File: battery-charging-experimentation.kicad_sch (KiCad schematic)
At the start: 23 parts, among them J1 USB_C_Receptacle_PowerOnly_6P, Q1 FS8205A, Q2 AO3415A, U2 DW01, U3 TP4056-42-ESOP8

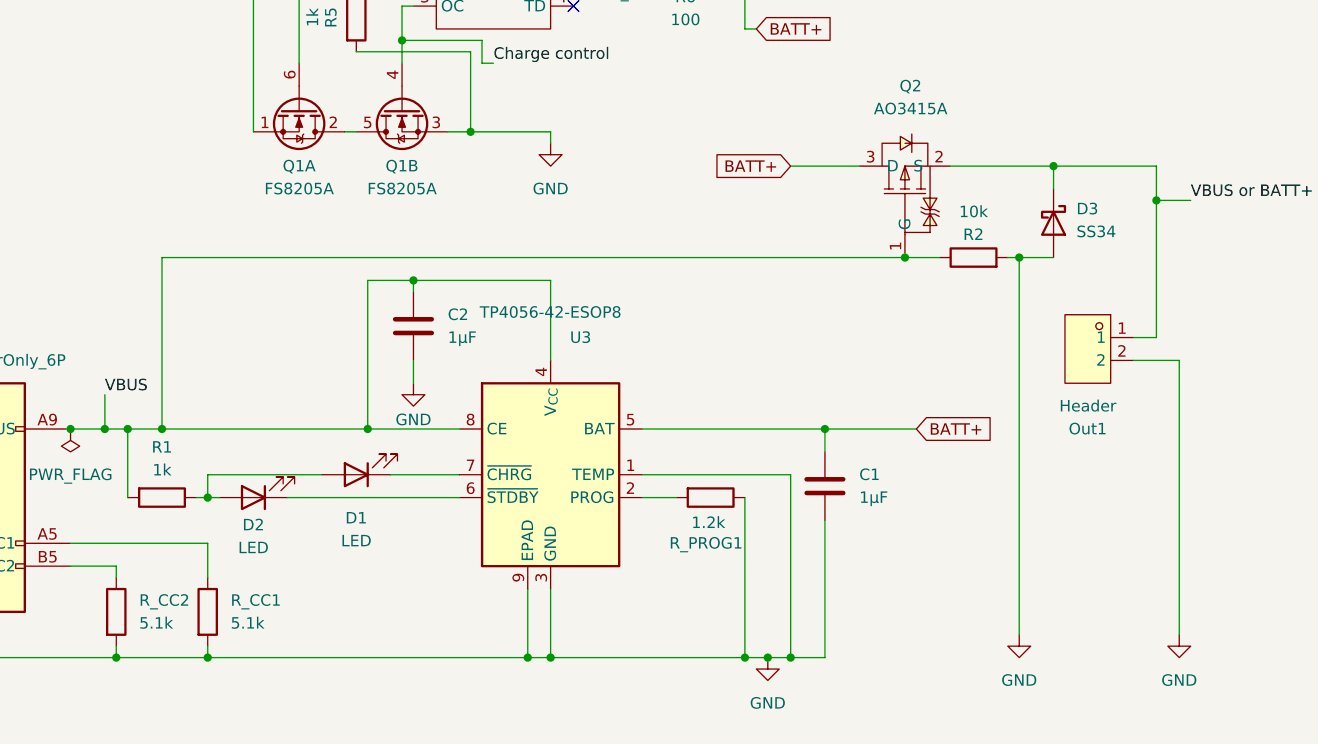
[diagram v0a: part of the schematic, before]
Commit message: move diode so the thing actually works
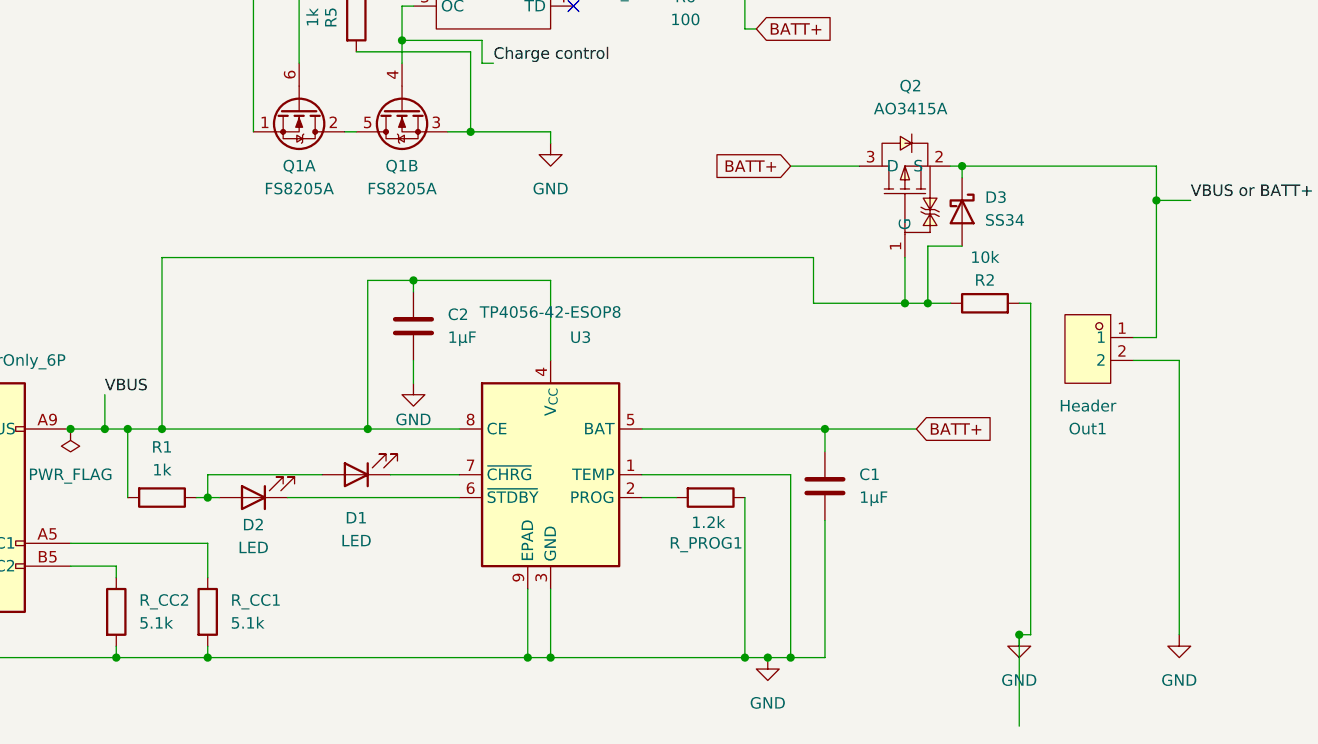
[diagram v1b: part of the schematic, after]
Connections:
- net GND: no longer D3.2 (A)
- net VBUS: now also D3.2 (A)
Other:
- title: (none) -> Chargey board
- moved on the sheet: D3, R2
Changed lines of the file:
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@@
 	(generator_version "9.0")
 	(paper "A4")
+	(title_block
+		(title "Chargey board")
+		(rev "2")
+	)
 	(junction
 		(at 33.02 190.5)
@@
 	)
 	(junction
-		(at 153.67 146.05)
-		(diameter 0)
-		(color 0 0 0 0)
-	)
-	(junction
 		(at 74.93 110.49)
 		(diameter 0)
@@
 	)
 	(junction
-		(at 140.97 146.05)
+		(at 143.51 151.13)
 		(diameter 0)
 		(color 0 0 0 0)
@@
 	)
 	(junction
-		(at 157.48 135.89)
+		(at 147.32 135.89)
 		(diameter 0)
 		(color 0 0 0 0)
@@
 	)
 	(junction
+		(at 153.67 187.96)
+		(diameter 0)
+		(color 0 0 0 0)
+	)
+	(junction
 		(at 101.6 190.5)
 		(diameter 0)
@@
 	)
 	(junction
+		(at 140.97 151.13)
+		(diameter 0)
+		(color 0 0 0 0)
+	)
+	(junction
 		(at 52.07 165.1)
 		(diameter 0)
@@
 	(wire
 		(pts
+			(xy 147.32 135.89) (xy 168.91 135.89)
+		)
+		(stroke
+			(width 0)
+			(type default)
+		)
+	)
+	(wire
+		(pts
 			(xy 68.58 102.87) (xy 68.58 132.08)
 		)
@@
 	(wire
 		(pts
-			(xy 146.05 135.89) (xy 157.48 135.89)
+			(xy 154.94 187.96) (xy 153.67 187.96)
 		)
 		(stroke
@@
 	(wire
 		(pts
-			(xy 90.17 132.08) (xy 92.71 132.08)
+			(xy 146.05 135.89) (xy 147.32 135.89)
 		)
 		(stroke
@@
 	(wire
 		(pts
-			(xy 123.19 120.65) (xy 123.19 114.3)
+			(xy 90.17 132.08) (xy 92.71 132.08)
 		)
 		(stroke
@@
 	(wire
 		(pts
-			(xy 93.98 121.92) (xy 85.09 121.92)
+			(xy 123.19 120.65) (xy 123.19 114.3)
 		)
 		(stroke
@@
 	(wire
 		(pts
-			(xy 157.48 146.05) (xy 153.67 146.05)
+			(xy 93.98 121.92) (xy 85.09 121.92)
 		)
 		(stroke
@@
 	(wire
 		(pts
+			(xy 147.32 144.78) (xy 143.51 144.78)
+		)
+		(stroke
+			(width 0)
+			(type default)
+		)
+	)
+	(wire
+		(pts
 			(xy 73.66 110.49) (xy 73.66 124.46)
 		)
@@
 	(wire
 		(pts
-			(xy 153.67 146.05) (xy 153.67 187.96)
+			(xy 143.51 144.78) (xy 143.51 151.13)
 		)
 		(stroke
@@
 	(wire
 		(pts
-			(xy 58.42 146.05) (xy 58.42 165.1)
+			(xy 130.81 146.05) (xy 130.81 151.13)
 		)
 		(stroke
@@
 	(wire
 		(pts
-			(xy 80.01 114.3) (xy 86.36 114.3)
+			(xy 58.42 146.05) (xy 58.42 165.1)
 		)
 		(stroke
@@
 	(wire
 		(pts
-			(xy 157.48 135.89) (xy 168.91 135.89)
+			(xy 80.01 114.3) (xy 86.36 114.3)
 		)
 		(stroke
@@
 	(wire
 		(pts
-			(xy 157.48 138.43) (xy 157.48 135.89)
+			(xy 147.32 137.16) (xy 147.32 135.89)
 		)
 		(stroke
@@
 	(wire
 		(pts
+			(xy 146.05 151.13) (xy 143.51 151.13)
+		)
+		(stroke
+			(width 0)
+			(type default)
+		)
+	)
+	(wire
+		(pts
+			(xy 130.81 151.13) (xy 140.97 151.13)
+		)
+		(stroke
+			(width 0)
+			(type default)
+		)
+	)
+	(wire
+		(pts
+			(xy 154.94 151.13) (xy 153.67 151.13)
+		)
+		(stroke
+			(width 0)
+			(type default)
+		)
+	)
+	(wire
+		(pts
 			(xy 132.08 190.5) (xy 128.27 190.5)
 		)
@@
 	(wire
 		(pts
-			(xy 140.97 146.05) (xy 144.78 146.05)
+			(xy 99.06 182.88) (xy 99.06 190.5)
 		)
 		(stroke
@@
 	(wire
 		(pts
-			(xy 99.06 182.88) (xy 99.06 190.5)
+			(xy 95.25 124.46) (xy 93.98 124.46)
 		)
 		(stroke
@@
 	(wire
 		(pts
-			(xy 95.25 124.46) (xy 93.98 124.46)
+			(xy 73.66 110.49) (xy 74.93 110.49)
 		)
 		(stroke
@@
 	(wire
 		(pts
-			(xy 73.66 110.49) (xy 74.93 110.49)
+			(xy 140.97 151.13) (xy 140.97 146.05)
 		)
 		(stroke
@@
 	(wire
 		(pts
-			(xy 58.42 146.05) (xy 140.97 146.05)
+			(xy 153.67 198.12) (xy 153.67 187.96)
 		)
 		(stroke
@@
 	(wire
 		(pts
+			(xy 58.42 146.05) (xy 130.81 146.05)
+		)
+		(stroke
+			(width 0)
+			(type default)
+		)
+	)
+	(wire
+		(pts
+			(xy 154.94 151.13) (xy 154.94 187.96)
+		)
+		(stroke
+			(width 0)
+			(type default)
+		)
+	)
+	(wire
+		(pts
 			(xy 52.07 161.29) (xy 52.07 165.1)
 		)
@@
 	(wire
 		(pts
-			(xy 152.4 146.05) (xy 153.67 146.05)
+			(xy 80.01 123.19) (xy 92.71 123.19)
 		)
 		(stroke
@@
 	(wire
 		(pts
-			(xy 80.01 123.19) (xy 92.71 123.19)
+			(xy 125.73 190.5) (xy 128.27 190.5)
 		)
 		(stroke
@@
 	(wire
 		(pts
-			(xy 125.73 190.5) (xy 128.27 190.5)
+			(xy 109.22 102.87) (xy 111.76 102.87)
 		)
 		(stroke
@@
 	(wire
 		(pts
-			(xy 109.22 102.87) (xy 111.76 102.87)
+			(xy 53.34 189.23) (xy 53.34 190.5)
 		)
 		(stroke
@@
 	(wire
 		(pts
-			(xy 53.34 189.23) (xy 53.34 190.5)
+			(xy 63.5 177.8) (xy 63.5 181.61)
 		)
 		(stroke
@@
 	(wire
 		(pts
-			(xy 63.5 177.8) (xy 63.5 181.61)
+			(xy 101.6 157.48) (xy 101.6 148.59)
 		)
 		(stroke
@@
 	(wire
 		(pts
-			(xy 101.6 157.48) (xy 101.6 148.59)
+			(xy 63.5 172.72) (xy 64.77 172.72)
 		)
 		(stroke
@@
 	(wire
 		(pts
-			(xy 63.5 172.72) (xy 64.77 172.72)
+			(xy 143.51 151.13) (xy 140.97 151.13)
 		)
 		(stroke
@@
 	(symbol
 		(lib_id "Diode:SS34")
-		(at 157.48 142.24 270)
+		(at 147.32 140.97 270)
 		(unit 1)
 		(exclude_from_sim no)
@@
 		(fields_autoplaced yes)
 		(property "Reference" "D3"
-			(at 160.02 140.6524 90)
+			(at 149.86 139.3824 90)
 			(effects
 				(font
@@
 		)
 		(property "Value" "SS34"
-			(at 160.02 143.1924 90)
+			(at 149.86 141.9224 90)
 			(effects
 				(font
@@
 		)
 		(property "Footprint" "easyeda2kicad:SMA_L4.3-W2.6-LS5.2-RD"
-			(at 153.035 142.24 0)
+			(at 142.875 140.97 0)
 			(effects
 				(font
@@
 		)
 		(property "Datasheet" "https://www.vishay.com/docs/88751/ss32.pdf"
-			(at 157.48 142.24 0)
+			(at 147.32 140.97 0)
 			(effects
 				(font
@@
 		)
 		(property "Description" "40V 3A Schottky Diode, SMA"
-			(at 157.48 142.24 0)
+			(at 147.32 140.97 0)
 			(effects
 				(font
@@
 		)
 		(property "LCSC Part" "C8678"
-			(at 157.48 142.24 90)
+			(at 147.32 140.97 90)
 			(effects
 				(font
@@
 	(symbol
 		(lib_id "Device:R")
-		(at 148.59 146.05 90)
+		(at 149.86 151.13 90)
 		(unit 1)
 		(exclude_from_sim no)
@@
 		(dnp no)
 		(property "Reference" "R2"
-			(at 148.59 143.51 90)
+			(at 149.86 148.59 90)
 			(effects
 				(font
@@
 		)
 		(property "Value" "10k"
-			(at 148.59 140.97 90)
+			(at 149.86 146.05 90)
 			(effects
 				(font
@@
 		)
 		(property "Footprint" "Resistor_SMD:R_0805_2012Metric_Pad1.20x1.40mm_HandSolder"
-			(at 148.59 147.828 90)
+			(at 149.86 152.908 90)
 			(effects
 				(font
@@
 		)
 		(property "Datasheet" "~"
-			(at 148.59 146.05 0)
+			(at 149.86 151.13 0)
 			(effects
 				(font
@@
 		)
 		(property "Description" "Resistor"
-			(at 148.59 146.05 0)
+			(at 149.86 151.13 0)
 			(effects
 				(font
@@
 		)
 		(property "LCSC Part" "C17414"
-			(at 148.59 146.05 90)
+			(at 149.86 151.13 90)
 			(effects
 				(font

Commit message: add a vbus out pin
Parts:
- Out1: footprint easyeda2kicad:HDR-TH_2P-P2.54-V-M -> Connector_PinHeader_2.54mm:PinHeader_1x03_P2.54mm_Vertical; symbol easyeda2kicad:HXPH254-01-02-Z-L11.5MALEHEADERCONNECTOR -> Connector:Conn_01x03_Pin
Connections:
- net VBUS: now also Out1.3 (Pin_3)
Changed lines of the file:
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@@
-	)
-	(junction
-		(at 168.91 139.7)
-		(diameter 0)
-		(color 0 0 0 0)
 	)
 	(junction
@@
 	)
 	(junction
+		(at 163.83 139.7)
+		(diameter 0)
+		(color 0 0 0 0)
+	)
+	(junction
 		(at 143.51 151.13)
 		(diameter 0)
@@
 	)
 	(junction
+		(at 130.81 151.13)
+		(diameter 0)
+		(color 0 0 0 0)
+	)
+	(junction
 		(at 123.19 102.87)
 		(diameter 0)
@@
 	)
 	(junction
-		(at 153.67 187.96)
-		(diameter 0)
-		(color 0 0 0 0)
-	)
-	(junction
 		(at 101.6 190.5)
 		(diameter 0)
@@
 	(wire
 		(pts
+			(xy 171.45 156.21) (xy 173.99 156.21)
+		)
+		(stroke
+			(width 0)
+			(type default)
+		)
+	)
+	(wire
+		(pts
 			(xy 123.19 106.68) (xy 123.19 102.87)
 		)
@@
 	(wire
 		(pts
+			(xy 171.45 156.21) (xy 171.45 187.96)
+		)
+		(stroke
+			(width 0)
+			(type default)
+		)
+	)
+	(wire
+		(pts
 			(xy 101.6 182.88) (xy 101.6 190.5)
 		)
@@
 	(wire
 		(pts
-			(xy 147.32 135.89) (xy 168.91 135.89)
+			(xy 147.32 135.89) (xy 163.83 135.89)
 		)
 		(stroke
@@
 	(wire
 		(pts
+			(xy 130.81 151.13) (xy 130.81 158.75)
+		)
+		(stroke
+			(width 0)
+			(type default)
+		)
+	)
+	(wire
+		(pts
 			(xy 90.17 132.08) (xy 92.71 132.08)
 		)
@@
 	(wire
 		(pts
-			(xy 171.45 187.96) (xy 171.45 157.48)
-		)
-		(stroke
-			(width 0)
-			(type default)
-		)
-	)
-	(wire
-		(pts
 			(xy 72.39 172.72) (xy 91.44 172.72)
 		)
@@
 	(wire
 		(pts
-			(xy 168.91 154.94) (xy 168.91 139.7)
+			(xy 163.83 153.67) (xy 163.83 139.7)
 		)
 		(stroke
@@
 	(wire
 		(pts
-			(xy 153.67 198.12) (xy 153.67 187.96)
-		)
-		(stroke
-			(width 0)
-			(type default)
-		)
-	)
-	(wire
-		(pts
-			(xy 168.91 154.94) (xy 166.37 154.94)
-		)
-		(stroke
-			(width 0)
-			(type default)
-		)
-	)
-	(wire
-		(pts
 			(xy 58.42 146.05) (xy 130.81 146.05)
 		)
@@
 	(wire
 		(pts
-			(xy 168.91 139.7) (xy 172.72 139.7)
-		)
-		(stroke
-			(width 0)
-			(type default)
-		)
-	)
-	(wire
-		(pts
 			(xy 25.4 190.5) (xy 33.02 190.5)
 		)
@@
 	(wire
 		(pts
-			(xy 171.45 157.48) (xy 166.37 157.48)
-		)
-		(stroke
-			(width 0)
-			(type default)
-		)
-	)
-	(wire
-		(pts
 			(xy 132.08 165.1) (xy 142.24 165.1)
 		)
@@
 	(wire
 		(pts
+			(xy 163.83 139.7) (xy 172.72 139.7)
+		)
+		(stroke
+			(width 0)
+			(type default)
+		)
+	)
+	(wire
+		(pts
 			(xy 53.34 190.5) (xy 63.5 190.5)
 		)
@@
 	(wire
 		(pts
+			(xy 130.81 158.75) (xy 173.99 158.75)
+		)
+		(stroke
+			(width 0)
+			(type default)
+		)
+	)
+	(wire
+		(pts
 			(xy 48.26 165.1) (xy 52.07 165.1)
 		)
@@
 	(wire
 		(pts
-			(xy 168.91 139.7) (xy 168.91 135.89)
+			(xy 163.83 139.7) (xy 163.83 135.89)
 		)
 		(stroke
@@
 		(pts
 			(xy 101.6 157.48) (xy 101.6 148.59)
+		)
+		(stroke
+			(width 0)
+			(type default)
+		)
+	)
+	(wire
+		(pts
+			(xy 163.83 153.67) (xy 173.99 153.67)
 		)
 		(stroke
@@
 	)
 	(symbol
-		(lib_id "easyeda2kicad:HXPH254-01-02-Z-L11.5MALEHEADERCONNECTOR")
-		(at 161.29 156.21 0)
+		(lib_id "Connector:Conn_01x03_Pin")
+		(at 179.07 156.21 0)
 		(mirror y)
 		(unit 1)
@@
 		(dnp no)
 		(property "Reference" "Out1"
-			(at 161.29 165.1 0)
+			(at 179.07 165.1 0)
 			(effects
 				(font
@@
 		)
 		(property "Value" "Header"
-			(at 161.29 162.56 0)
+			(at 179.07 162.56 0)
 			(effects
 				(font
@@
 			)
 		)
-		(property "Footprint" "easyeda2kicad:HDR-TH_2P-P2.54-V-M"
-			(at 161.29 165.1 0)
+		(property "Footprint" "Connector_PinHeader_2.54mm:PinHeader_1x03_P2.54mm_Vertical"
+			(at 179.07 156.21 0)
 			(effects
 				(font
@@
 			)
 		)
-		(property "Datasheet" ""
-			(at 161.29 156.21 0)
+		(property "Datasheet" "~"
+			(at 179.07 156.21 0)
 			(effects
 				(font
@@
 			)
 		)
-		(property "Description" ""
-			(at 161.29 156.21 0)
+		(property "Description" "Generic connector, single row, 01x03, script generated"
+			(at 179.07 156.21 0)
 			(effects
 				(font
@@
 		)
 		(property "LCSC Part" "C52016390"
-			(at 161.29 167.64 0)
+			(at 179.07 167.64 0)
 			(effects
 				(font
@@
 		(pin "2"
 		)
+		(pin "3"
+		)
 		(instances

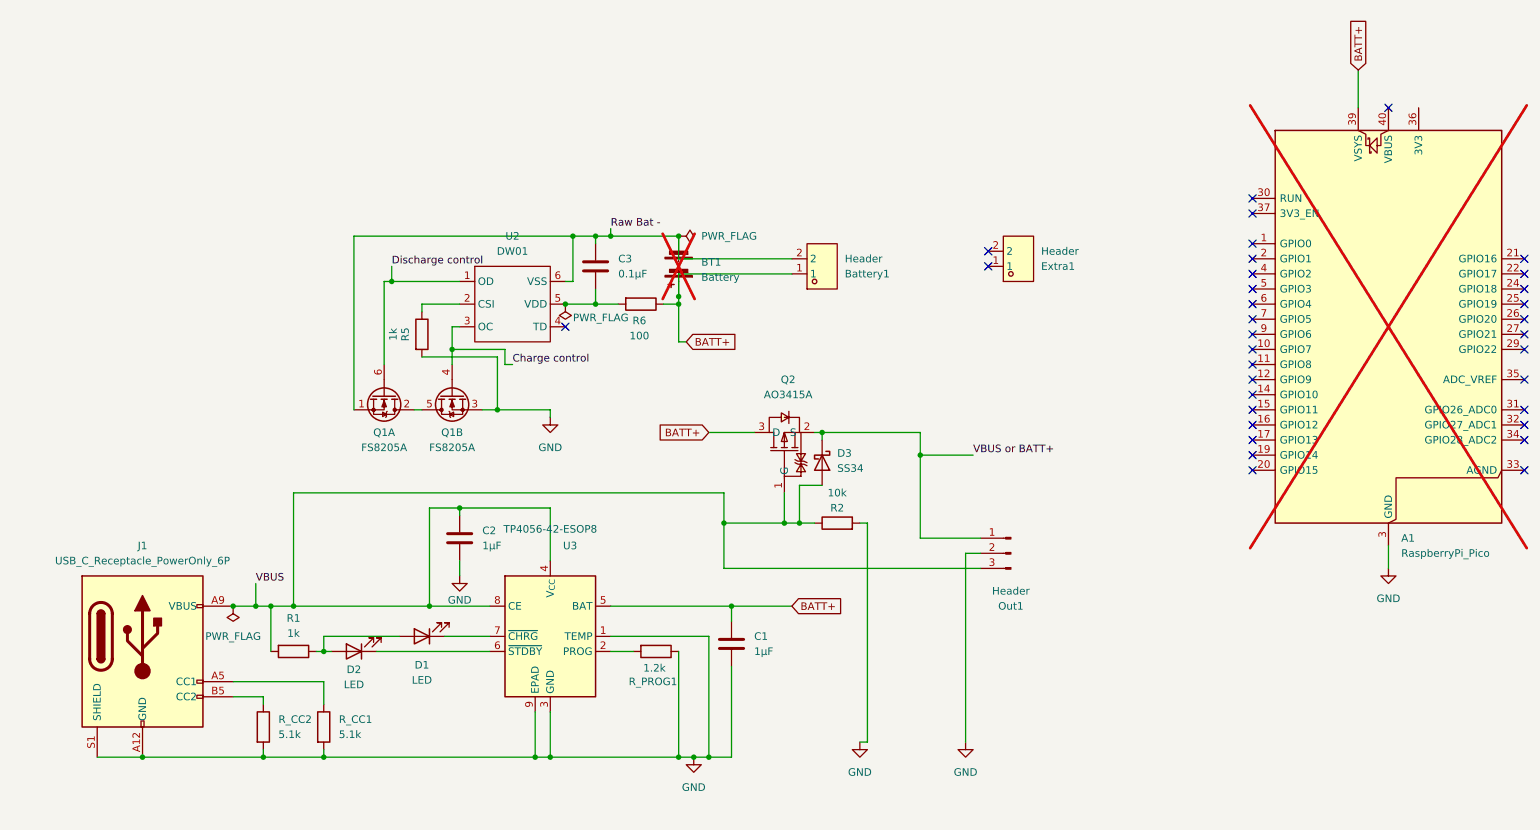
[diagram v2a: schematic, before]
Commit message: smaller components, power from pico USB port
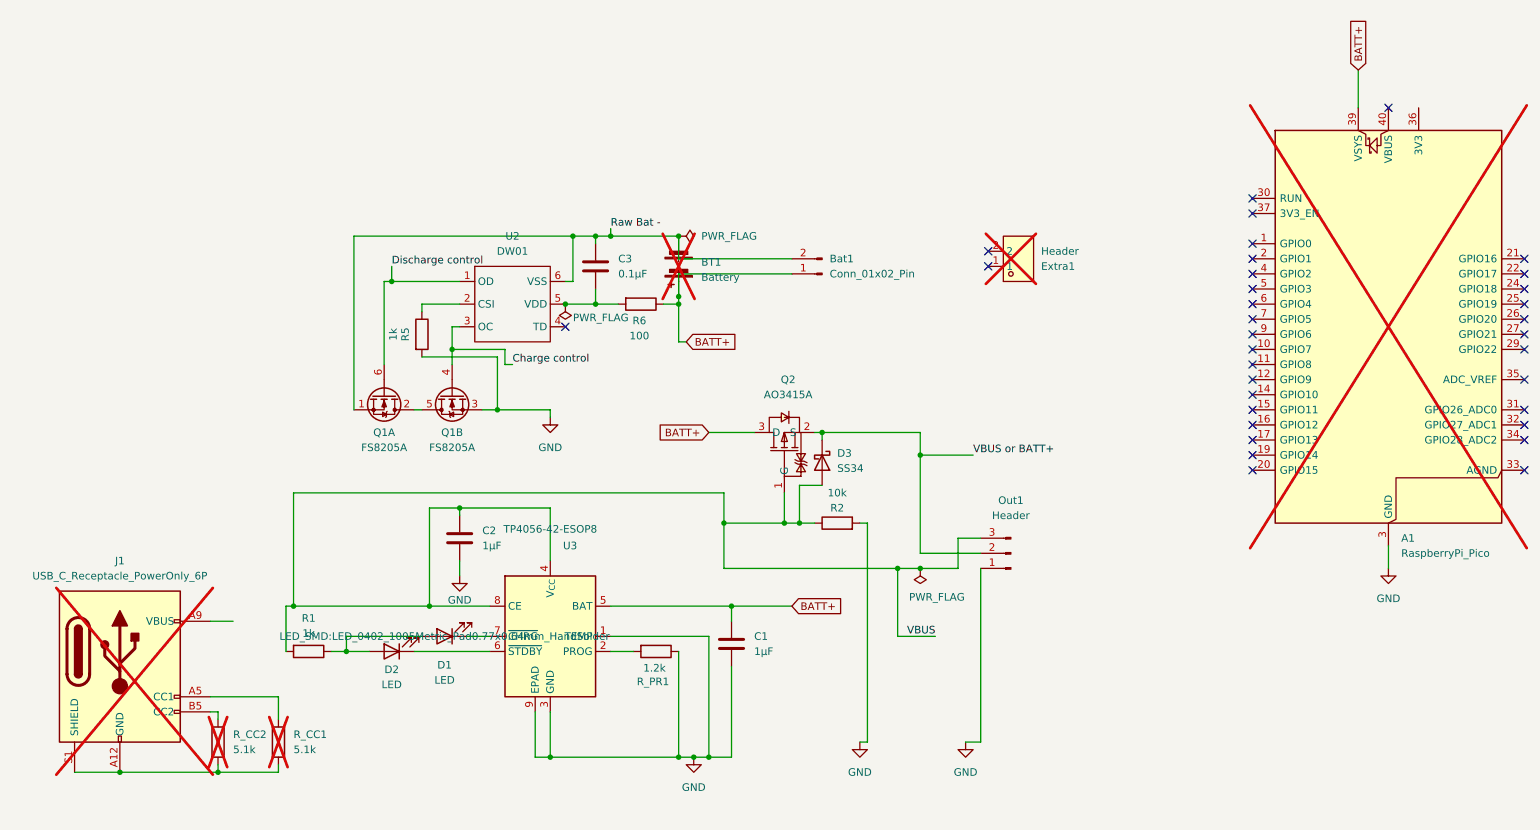
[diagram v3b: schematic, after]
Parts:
- removed Battery1: Header, easyeda2kicad:HDR-TH_2P-P2.54-V-M, symbol easyeda2kicad:HXPH254-01-02-Z-L11.5MALEHEADERCONNECTOR
- added Bat1: Conn_01x02_Pin, Connector_PinHeader_2.54mm:PinHeader_1x02_P2.54mm_Vertical, symbol Connector:Conn_01x02_Pin
- C1, C2, C3: footprint Capacitor_SMD:C_0805_2012Metric_Pad1.18x1.45mm_HandSolder -> Capacitor_SMD:C_0402_1005Metric_Pad0.74x0.62mm_HandSolder
- D1, D2: footprint LED_SMD:LED_0805_2012Metric_Pad1.15x1.40mm_HandSolder -> LED_SMD:LED_0402_1005Metric_Pad0.77x0.64mm_HandSolder
- Extra1, R_CC1, R_CC2: now not fitted; now left out of the parts list
- J1: now not fitted
- R1, R2, R5, R6: footprint Resistor_SMD:R_0805_2012Metric_Pad1.20x1.40mm_HandSolder -> Resistor_SMD:R_0402_1005Metric_Pad0.72x0.64mm_HandSolder
- R_PR1: renamed from R_PROG1; footprint Resistor_SMD:R_0805_2012Metric_Pad1.20x1.40mm_HandSolder -> Resistor_SMD:R_0402_1005Metric_Pad0.72x0.64mm_HandSolder
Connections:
- net BATT+: now also Bat1.1 (Pin_1)
- net GND: now also Out1.1 (Pin_1); no longer J1.A12 (GND), J1.B12 (GND), J1.S1 (SHIELD), Out1.2 (Pin_2), R_CC1.2, R_CC2.2
- net Raw Bat -: now also Bat1.2 (Pin_2)
- net VBUS: no longer J1.A9 (VBUS), J1.B9 (VBUS)
- net VBUS or BATT+: now also Out1.2 (Pin_2); no longer Out1.1 (Pin_1)
- new net: J1.A12 (GND), J1.B12 (GND), J1.S1 (SHIELD), R_CC1.2, R_CC2.2
- new net: J1.A9 (VBUS), J1.B9 (VBUS)
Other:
- moved on the sheet: D1, D2, Out1, R1
